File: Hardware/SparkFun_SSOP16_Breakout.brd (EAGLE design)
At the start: 25.4 x 12.7 mm, 4 parts, among them U1 SSOP16

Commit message: Updated board files
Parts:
- removed U$1: LOGO-SFESK, SparkFun:SFE-LOGO-FLAME
- added FRAME1: FRAME-LETTER, SparkFun-Aesthetics:CREATIVE_COMMONS
- added LOGO1: SFE_LOGO_FLAME.1_INCH, SparkFun-Aesthetics:SFE_LOGO_FLAME_.1
- added LOGO3: OSHW-LOGOS, SparkFun-Aesthetics:OSHW-LOGO-S
- JP1: device SparkFun:1X08 -> SparkFun-Connectors:1X08_PIN1_NO_SILK
- JP2: device SparkFun:1X08 -> SparkFun-Connectors:1X08_NO_SILK
- U1: device SparkFun:SSOP16 -> generic-ssop16:SSOP16
- moved JP2 3.59 mm to (1.27, 8.89)
- moved U1 2.84 mm to (10.2, 5.08)
- moved JP1 2.54 mm to (1.27, 1.27)
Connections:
- net N$1: now also U1.P$1; no longer U1.P$8
- net N$2: now also U1.P$2; no longer U1.P$7
- net N$3: now also U1.P$3; no longer U1.P$6
- net N$4: now also U1.P$4; no longer U1.P$5
- net N$5: now also U1.P$5; no longer U1.P$4
- net N$6: now also U1.P$6; no longer U1.P$3
- net N$7: now also U1.P$7; no longer U1.P$2
- net N$8: now also U1.P$8; no longer U1.P$1
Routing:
- net N$4: track 6.28 -> 11.6 mm, vias 0 -> 1
- net N$8: track 20.2 -> 15.2 mm
- net N$7: track 16.4 -> 11.7 mm
- net N$2: track 6.46 -> 10.3 mm, vias 1 -> 0
- net N$3: track 7.52 -> 11.3 mm, vias 1 -> 0
- net N$1: track 7.67 -> 10.4 mm
- net N$5: track 8.12 -> 10.2 mm, vias 0 -> 1
- net N$16: track 12.4 -> 10.4 mm
- net N$12: track 8.30 -> 10.2 mm
- net N$6: track 10.7 -> 8.86 mm, vias 0 -> 1
- net N$14: track 9.60 -> 11.3 mm
- net N$13: track 9.98 -> 11.6 mm, vias 0 -> 1
- net N$10: track 13.2 -> 11.7 mm
- net N$9: track 13.8 -> 15.2 mm, vias 0 -> 1
- net N$15: track 10.9 -> 10.3 mm
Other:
- board size 25.4 x 12.7 mm -> 20.3 x 10.2 mm
- board text added: "Byron Jacquot"
- board text added: "SSOP16 to DIP16"
- board text removed: "16"
- board text removed: "SSOP16"

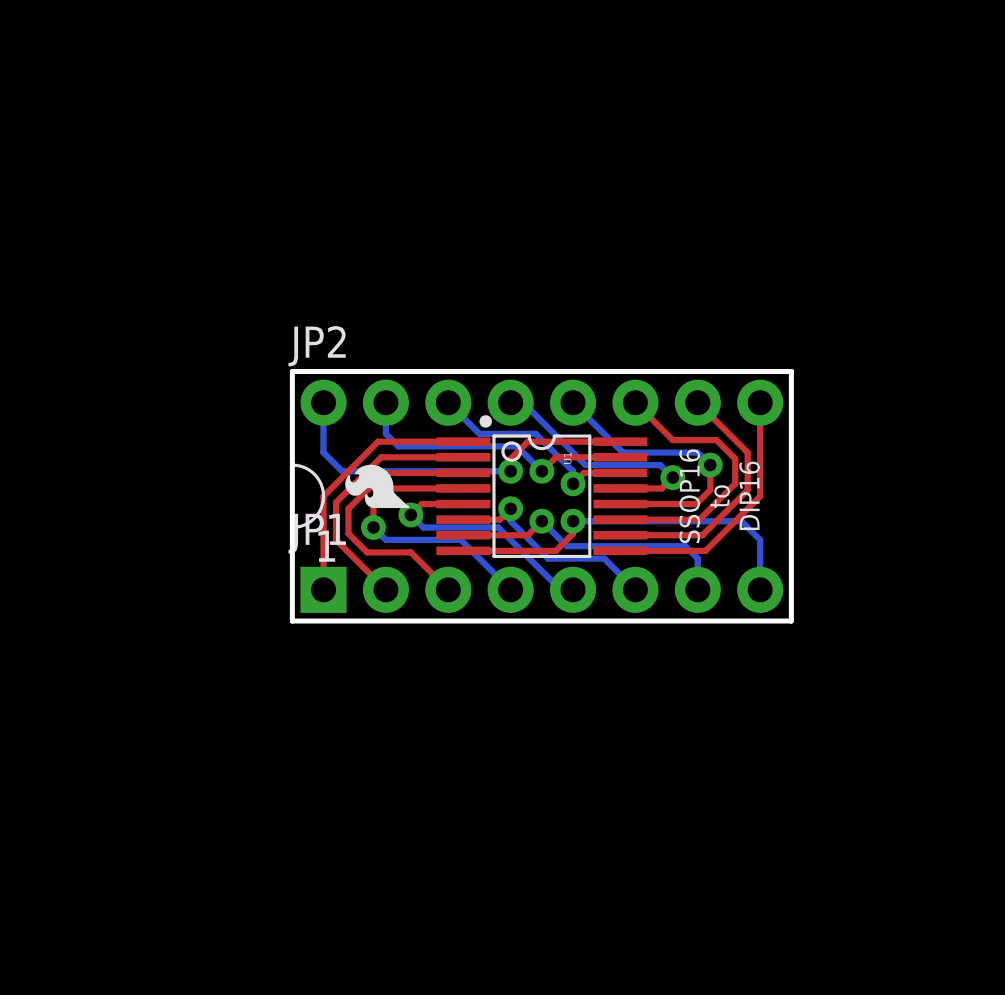
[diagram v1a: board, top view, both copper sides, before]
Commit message: Moving towards actual design.
-2-up panel.
-Dimensioning added.
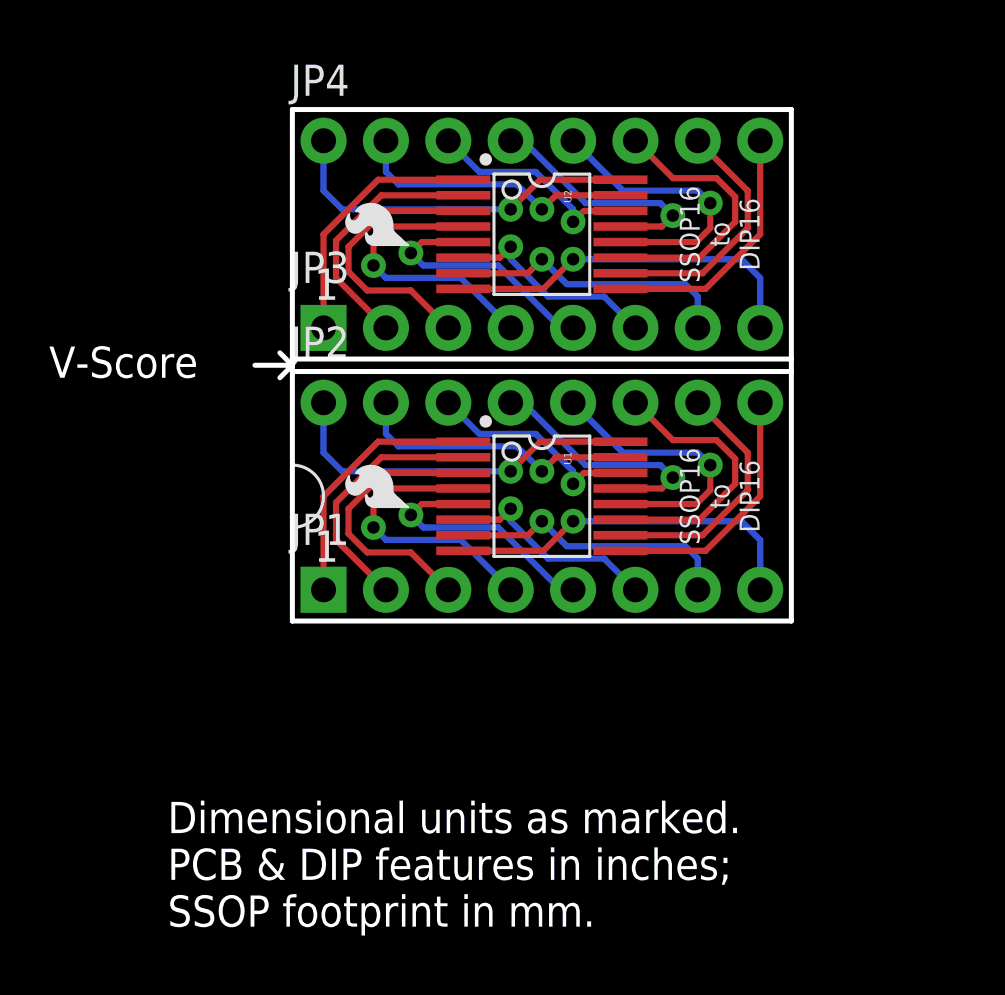
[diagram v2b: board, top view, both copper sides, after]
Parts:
- added JP3: (no value), SparkFun-Connectors:1X08_PIN1_NO_SILK
- added JP4: (no value), SparkFun-Connectors:1X08_NO_SILK
- added LOGO2: SFE_LOGO_FLAME.1_INCH, SparkFun-Aesthetics:SFE_LOGO_FLAME_.1
- added LOGO4: OSHW-LOGOS, SparkFun-Aesthetics:OSHW-LOGO-S
- added U2: SSOP16, generic-ssop16:SSOP16
- moved FRAME1 16.1 mm to (-19.8, -20.8)
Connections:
- new net N$17: JP4.1, U2.P$16
- new net N$18: JP4.2, U2.P$15
- new net N$19: JP4.3, U2.P$14
- new net N$20: JP4.4, U2.P$13
- new net N$21: JP4.5, U2.P$12
- new net N$22: JP4.6, U2.P$11
- new net N$23: JP4.7, U2.P$10
- new net N$24: JP4.8, U2.P$9
- new net N$25: JP3.1, U2.P$1
- new net N$26: JP3.2, U2.P$2
- new net N$27: JP3.3, U2.P$3
- new net N$28: JP3.4, U2.P$4
- new net N$29: JP3.5, U2.P$5
- new net N$30: JP3.6, U2.P$6
- new net N$31: JP3.7, U2.P$7
- new net N$32: JP3.8, U2.P$8
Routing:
- net N$17: track 0.00 -> 14.9 mm, vias 0 -> 1
- net N$32: track 0.00 -> 14.9 mm, vias 0 -> 1
- net N$18: track 0.00 -> 11.7 mm, vias 0 -> 1
- net N$31: track 0.00 -> 11.7 mm, vias 0 -> 1
- net N$21: track 0.00 -> 11.6 mm, vias 0 -> 1
- net N$28: track 0.00 -> 11.6 mm, vias 0 -> 1
- net N$27: track 0.00 -> 11.3 mm
- net N$22: track 0.00 -> 11.3 mm
- net N$24: track 0.00 -> 10.4 mm
- net N$25: track 0.00 -> 10.4 mm
- net N$23: track 0.00 -> 10.3 mm
- net N$26: track 0.00 -> 10.3 mm
- net N$29: track 0.00 -> 10.2 mm, vias 0 -> 1
- net N$20: track 0.00 -> 10.2 mm, vias 0 -> 1
- net N$30: track 0.00 -> 8.86 mm, vias 0 -> 1
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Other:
- board size 20.3 x 10.2 mm -> 21.8 x 20.8 mm
- board text added: "Dimensional units as marked. PCB & DIP features in inches; SSOP footprint in mm."
- board text added: "V-Score"
